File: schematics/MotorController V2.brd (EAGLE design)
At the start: 120.6 x 100 mm, 40 parts, among them IC1 7805, Q1 BC307

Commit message: AfterWeekend
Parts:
- removed HALL1, HALL2, HALL3: (no value), con-molex-micro-fit-3_0:43045-0612
- added D10, D11, D12, D13, D4, D5, D6, D7, D8, D9: 5.1V, diode:DO41Z10
- added D3: 1N5818-B, diode:DO41-7.6
- added R12, R13, R14: 1K, resistor:0204/7
- C1: value 2200uF -> 1000uF; device rcl:E7,5-16 -> rcl:E5-10,5
- C2: value 2200uF -> 100uF; device rcl:E7,5-16 -> rcl:E5-5
- CONTROL, S1, S2: value (none) -> (none)
- R1, R2, R3: value 330 -> 1K
- moved C3 79.2 mm to (0.00, 1.27), turned to 90 degrees
- moved R7 53.2 mm to (-34.9, 3.81), turned to 0 degrees
- moved R8 53.2 mm to (-34.9, 6.35), turned to 0 degrees
- moved R9 53.2 mm to (-34.9, 8.89), turned to 0 degrees
- moved R6 32.5 mm to (-35.6, 39.4), turned to 0 degrees
- moved R4 32.5 mm to (-35.6, 34.3), turned to 0 degrees
- moved R5 32.5 mm to (-35.6, 36.8), turned to 0 degrees
- moved IC1 22.2 mm to (8.89, 2.54), turned to 270 degrees
- moved R3 17.3 mm to (-35.6, 69.8), turned to 0 degrees
- moved R1 17.3 mm to (-35.6, 64.8), turned to 0 degrees
- moved R2 17.3 mm to (-35.6, 67.3), turned to 0 degrees
- moved C2 14.9 mm to (-2.54, -5.08), turned to 0 degrees
- moved POWER_IN 7.62 mm to (-16.5, -5.08)
- moved R11 6.35 mm to (-22.9, -5.08)
- moved U$2 5.39 mm to (11.4, 22.9), turned to 180 degrees
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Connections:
- net LCTRL-GND renamed CTRL-GND
- net N$48 renamed IMU-INT
- removed net LCTR-RX: CONTROL.6, U$2.HV4
- removed net LCTRL-SCL: CONTROL.4, U$2.HV2
- removed net LCTRL-SDA: CONTROL.3, U$2.HV1
- removed net LCTRL-TX: CONTROL.5, U$2.HV3
- removed net LCTRL-VDD: CONTROL.2, U$2.HV
- removed net LV: U$2.LV
- removed net N$49: HALL3.P$2, PRJ1.23/A9
- removed net N$50: HALL3.P$3, PRJ1.22/A8
- removed net N$51: HALL2.P$2, PRJ1.21/A7
- removed net N$54: HALL1.P$1, PRJ1.17/A3
- removed net N$55: HALL2.P$1, PRJ1.16/A2
- removed net N$56: HALL3.P$1, PRJ1.15/A1
- removed net N$57: HALL1.P$2, PRJ1.1/TX
- removed net N$58: HALL1.P$3, PRJ1.14/A0
- removed net N$59: HALL2.P$3, PRJ1.13/SCK
- new net CTR-SCL: CONTROL.4, U$2.LV1
- new net CTR-SDA: CONTROL.3, U$2.LV2
- new net CTRL-RX: CONTROL.6, U$2.LV4
- new net CTRL-TX: CONTROL.5, U$2.LV3
- new net CTRL-VDD: CONTROL.2, U$2.LV
- new net N$43: DRK1.EN, R12.2
- new net N$46: D4.C, PRJ1.24, R12.1, R13.1, R14.1
- new net N$48: DRK2.EN, R13.2
- net 3.3V: now also U$2.HV; no longer HALL1.P$5, HALL2.P$5, HALL3.P$5
- net GND: now also D10.A, D11.A, D12.A, D13.A, D4.A, D5.A, D6.A, D7.A, D8.A, D9.A; no longer HALL1.P$4, HALL2.P$4, HALL3.P$4
- net IMU-SCL: now also PRJ1.18/A4/SDA; no longer PRJ1.19/A5/SCL
- net IMU-SDA: now also PRJ1.19/A5/SCL; no longer PRJ1.18/A4/SDA
- net N$10: now also R14.2; no longer DRK1.EN, DRK2.EN, PRJ1.24
- net N$21: now also D8.C
- net N$22: now also D9.C
- net N$23: now also D10.C
- net N$27: now also D11.C
- net N$28: now also D12.C
- net N$29: now also D13.C
- net N$32: now also D3.C
- net N$34: now also ENCODER1.1; no longer ENCODER1.2
- net N$36: now also ENCODER2.1; no longer ENCODER2.2
- net N$38: now also ENCODER3.1; no longer ENCODER3.2
- net N$7: now also D7.C
- net N$8: now also D6.C
- net N$9: now also D5.C
- net RX5: now also U$2.HV4; no longer U$2.LV4
- net SCL1: now also U$2.HV1; no longer U$2.LV1
- net SDA1: now also U$2.HV2; no longer U$2.LV2
- net TX5: now also U$2.HV3; no longer U$2.LV3
- net VCC: now also D3.A, ENCODER1.2, ENCODER2.2, ENCODER3.2; no longer ENCODER1.1, ENCODER2.1, ENCODER3.1
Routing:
- net N$50: track 261.6 -> 0.00 mm, vias 3 -> 0
- net 3.3V: track 315.4 -> 105.4 mm, vias 3 -> 2
- net N$56: track 200.8 -> 0.00 mm, vias 3 -> 0
- net N$49: track 175.8 -> 0.00 mm, vias 3 -> 0
- net N$59: track 164.9 -> 0.00 mm, vias 3 -> 0
- net N$27: track 6.68 -> 164.7 mm
- net N$55: track 153.5 -> 0.00 mm, vias 1 -> 0
- net N$46: track 0.00 -> 139.6 mm, vias 0 -> 1
- net N$58: track 118.5 -> 0.00 mm, vias 3 -> 0
- net N$51: track 114.9 -> 0.00 mm, vias 3 -> 0
- net N$57: track 113.5 -> 0.00 mm, vias 2 -> 0
- net N$54: track 112.2 -> 0.00 mm, vias 2 -> 0
- net N$10: track 92.0 -> 2.08 mm, vias 2 -> 0
- net N$28: track 6.70 -> 78.9 mm, vias 0 -> 3
- net N$44: track 103.9 -> 175.1 mm, vias 2 -> 0
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
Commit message: no message
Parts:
- D10, D11, D12, D13, D4, D5, D6, D7, D8, D9: value 5.1V -> 5.6V
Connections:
- removed net N$41: PRJ1.32/A13, U$1.VDD
- net LIPO-GND: no longer U$1.D1
- net VCC: no longer U$1.!D2
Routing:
- net N$41: track 135.4 -> 0.00 mm, vias 3 -> 0
- net LIPO-GND: track 266.0 -> 263.1 mm
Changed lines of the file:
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@@
 <element name="D3" library="diode" library_urn="urn:adsk.eagle:library:210" package="DO41-7.6" package3d_urn="urn:adsk.eagle:package:43421/1" value="1N5818-B" x="-9.525" y="1.27"/>
 <element name="R12" library="resistor" library_urn="urn:adsk.eagle:library:348" package="0204/7" package3d_urn="urn:adsk.eagle:package:23498/1" value="1K" x="-35.56" y="72.39"/>
-<element name="D4" library="diode" library_urn="urn:adsk.eagle:library:210" package="DO41Z10" package3d_urn="urn:adsk.eagle:package:43341/1" value="5.1V" x="-46.355" y="72.39" rot="R180"/>
-<element name="D5" library="diode" library_urn="urn:adsk.eagle:library:210" package="DO41Z10" package3d_urn="urn:adsk.eagle:package:43341/1" value="5.1V" x="-46.355" y="69.85" rot="R180"/>
-<element name="D6" library="diode" library_urn="urn:adsk.eagle:library:210" package="DO41Z10" package3d_urn="urn:adsk.eagle:package:43341/1" value="5.1V" x="-46.355" y="67.31" rot="R180"/>
-<element name="D7" library="diode" library_urn="urn:adsk.eagle:library:210" package="DO41Z10" package3d_urn="urn:adsk.eagle:package:43341/1" value="5.1V" x="-46.355" y="64.77" rot="R180"/>
+<element name="D4" library="diode" library_urn="urn:adsk.eagle:library:210" package="DO41Z10" package3d_urn="urn:adsk.eagle:package:43341/1" value="5.6V" x="-46.355" y="72.39" rot="R180"/>
+<element name="D5" library="diode" library_urn="urn:adsk.eagle:library:210" package="DO41Z10" package3d_urn="urn:adsk.eagle:package:43341/1" value="5.6V" x="-46.355" y="69.85" rot="R180"/>
+<element name="D6" library="diode" library_urn="urn:adsk.eagle:library:210" package="DO41Z10" package3d_urn="urn:adsk.eagle:package:43341/1" value="5.6V" x="-46.355" y="67.31" rot="R180"/>
+<element name="D7" library="diode" library_urn="urn:adsk.eagle:library:210" package="DO41Z10" package3d_urn="urn:adsk.eagle:package:43341/1" value="5.6V" x="-46.355" y="64.77" rot="R180"/>
 <element name="R13" library="resistor" library_urn="urn:adsk.eagle:library:348" package="0204/7" package3d_urn="urn:adsk.eagle:package:23498/1" value="1K" x="-35.56" y="41.91"/>
 <element name="R14" library="resistor" library_urn="urn:adsk.eagle:library:348" package="0204/7" package3d_urn="urn:adsk.eagle:package:23498/1" value="1K" x="-34.925" y="11.43"/>
-<element name="D8" library="diode" library_urn="urn:adsk.eagle:library:210" package="DO41Z10" package3d_urn="urn:adsk.eagle:package:43341/1" value="5.1V" x="-46.355" y="39.37" rot="R180"/>
-<element name="D9" library="diode" library_urn="urn:adsk.eagle:library:210" package="DO41Z10" package3d_urn="urn:adsk.eagle:package:43341/1" value="5.1V" x="-46.355" y="36.83" rot="R180"/>
-<element name="D10" library="diode" library_urn="urn:adsk.eagle:library:210" package="DO41Z10" package3d_urn="urn:adsk.eagle:package:43341/1" value="5.1V" x="-46.355" y="34.29" rot="R180"/>
-<element name="D11" library="diode" library_urn="urn:adsk.eagle:library:210" package="DO41Z10" package3d_urn="urn:adsk.eagle:package:43341/1" value="5.1V" x="-46.355" y="8.89" rot="R180"/>
-<element name="D12" library="diode" library_urn="urn:adsk.eagle:library:210" package="DO41Z10" package3d_urn="urn:adsk.eagle:package:43341/1" value="5.1V" x="-46.355" y="6.35" rot="R180"/>
-<element name="D13" library="diode" library_urn="urn:adsk.eagle:library:210" package="DO41Z10" package3d_urn="urn:adsk.eagle:package:43341/1" value="5.1V" x="-46.355" y="3.81" rot="R180"/>
+<element name="D8" library="diode" library_urn="urn:adsk.eagle:library:210" package="DO41Z10" package3d_urn="urn:adsk.eagle:package:43341/1" value="5.6V" x="-46.355" y="39.37" rot="R180"/>
+<element name="D9" library="diode" library_urn="urn:adsk.eagle:library:210" package="DO41Z10" package3d_urn="urn:adsk.eagle:package:43341/1" value="5.6V" x="-46.355" y="36.83" rot="R180"/>
+<element name="D10" library="diode" library_urn="urn:adsk.eagle:library:210" package="DO41Z10" package3d_urn="urn:adsk.eagle:package:43341/1" value="5.6V" x="-46.355" y="34.29" rot="R180"/>
+<element name="D11" library="diode" library_urn="urn:adsk.eagle:library:210" package="DO41Z10" package3d_urn="urn:adsk.eagle:package:43341/1" value="5.6V" x="-46.355" y="8.89" rot="R180"/>
+<element name="D12" library="diode" library_urn="urn:adsk.eagle:library:210" package="DO41Z10" package3d_urn="urn:adsk.eagle:package:43341/1" value="5.6V" x="-46.355" y="6.35" rot="R180"/>
+<element name="D13" library="diode" library_urn="urn:adsk.eagle:library:210" package="DO41Z10" package3d_urn="urn:adsk.eagle:package:43341/1" value="5.6V" x="-46.355" y="3.81" rot="R180"/>
 </elements>
 <signals>
@@
 <contactref element="Q1" pad="1"/>
 <contactref element="U$1" pad="VIN"/>
-<contactref element="U$1" pad="!D2"/>
 <contactref element="ENCODER3" pad="2"/>
 <contactref element="ENCODER2" pad="2"/>
@@
 <wire x1="7.112" y1="66.675" x2="8.89" y2="64.897" width="0.254" layer="16"/>
 <wire x1="7.112" y1="77.56525" x2="7.112" y2="66.675" width="0.254" layer="16"/>
-<wire x1="8.89" y1="64.897" x2="8.89" y2="64.77" width="0.254" layer="16"/>
 <wire x1="25.3365" y1="50.673" x2="25.3365" y2="39.5605" width="0.254" layer="1"/>
 <wire x1="11.33475" y1="64.67475" x2="25.3365" y2="50.673" width="0.254" layer="1"/>
 <wire x1="8.89" y1="64.67475" x2="11.33475" y2="64.67475" width="0.254" layer="1"/>
 <wire x1="25.3365" y1="39.5605" x2="25.4" y2="39.37" width="0.254" layer="1"/>
-<wire x1="8.89" y1="64.67475" x2="8.89" y2="64.77" width="0.254" layer="1"/>
 <wire x1="24.66975" y1="0" x2="5.08" y2="0" width="0.254" layer="1"/>
 <wire x1="40.4495" y1="15.77975" x2="24.66975" y2="0" width="0.254" layer="1"/>
@@
 <via x="12.446" y="74.45375" extent="1-16" drill="0.635"/>
 <via x="-21.11375" y="-8.22325" extent="1-16" drill="0.635"/>
+<wire x1="8.89" y1="64.67475" x2="8.89" y2="64.897" width="0" layer="19" extent="1-16"/>
 </signal>
 <signal name="GND">
@@
 <wire x1="30.226" y1="58.45175" x2="30.099" y2="58.293" width="1" layer="1"/>
 </signal>
-<signal name="N$41">
-<contactref element="PRJ1" pad="32/A13"/>
-<contactref element="U$1" pad="VDD"/>
-<wire x1="-3.33375" y1="18.89125" x2="-15.113" y2="18.89125" width="0.254" layer="16"/>
-<wire x1="2.44475" y1="13.11275" x2="-3.33375" y2="18.89125" width="0.254" layer="16"/>
-<wire x1="39.116" y1="13.11275" x2="2.44475" y2="13.11275" width="0.254" layer="16"/>
-<wire x1="41.3385" y1="15.33525" x2="39.116" y2="13.11275" width="0.254" layer="16"/>
-<wire x1="41.3385" y1="28.8925" x2="41.3385" y2="15.33525" width="0.254" layer="16"/>
-<wire x1="39.33825" y1="30.89275" x2="41.3385" y2="28.8925" width="0.254" layer="16"/>
-<wire x1="34.671" y1="30.89275" x2="39.33825" y2="30.89275" width="0.254" layer="16"/>
-<wire x1="30.89275" y1="30.89275" x2="34.671" y2="30.89275" width="0.254" layer="1"/>
-<wire x1="23.114" y1="38.6715" x2="30.89275" y2="30.89275" width="0.254" layer="1"/>
-<wire x1="23.114" y1="50.89525" x2="23.114" y2="38.6715" width="0.254" layer="1"/>
-<wire x1="23.114" y1="58.00725" x2="23.114" y2="50.89525" width="0.254" layer="16"/>
-<wire x1="8.89" y1="72.23125" x2="23.114" y2="58.00725" width="0.254" layer="1"/>
-<wire x1="-15.113" y1="18.89125" x2="-15.24" y2="19.05" width="0.254" layer="16"/>
-<wire x1="8.89" y1="72.23125" x2="8.89" y2="72.39" width="0.254" layer="1"/>
-<via x="34.671" y="30.89275" extent="1-16" drill="0.635"/>
-<via x="23.114" y="50.89525" extent="1-16" drill="0.635"/>
-<via x="23.114" y="58.00725" extent="1-16" drill="0.635"/>
-</signal>
 <signal name="CTRL-RX">
 <contactref element="CONTROL" pad="6"/>
@@
 <contactref element="R11" pad="1"/>
 <contactref element="U$1" pad="GND"/>
-<contactref element="U$1" pad="D1"/>
 <wire x1="21.7805" y1="61.56325" x2="30.00375" y2="61.56325" width="1" layer="16"/>
 <wire x1="17.11325" y1="56.896" x2="21.7805" y2="61.56325" width="1" layer="16"/>
 <wire x1="11.77925" y1="62.23" x2="17.11325" y2="56.896" width="1" layer="1"/>
-<wire x1="8.89" y1="62.23" x2="11.77925" y2="62.23" width="1" layer="1"/>
 <wire x1="30.00375" y1="61.56325" x2="30.099" y2="61.722" width="1" layer="16"/>
 <wire x1="-38.6715" y1="-5.55625" x2="-38.6715" y2="-4.8895" width="1" layer="1"/>

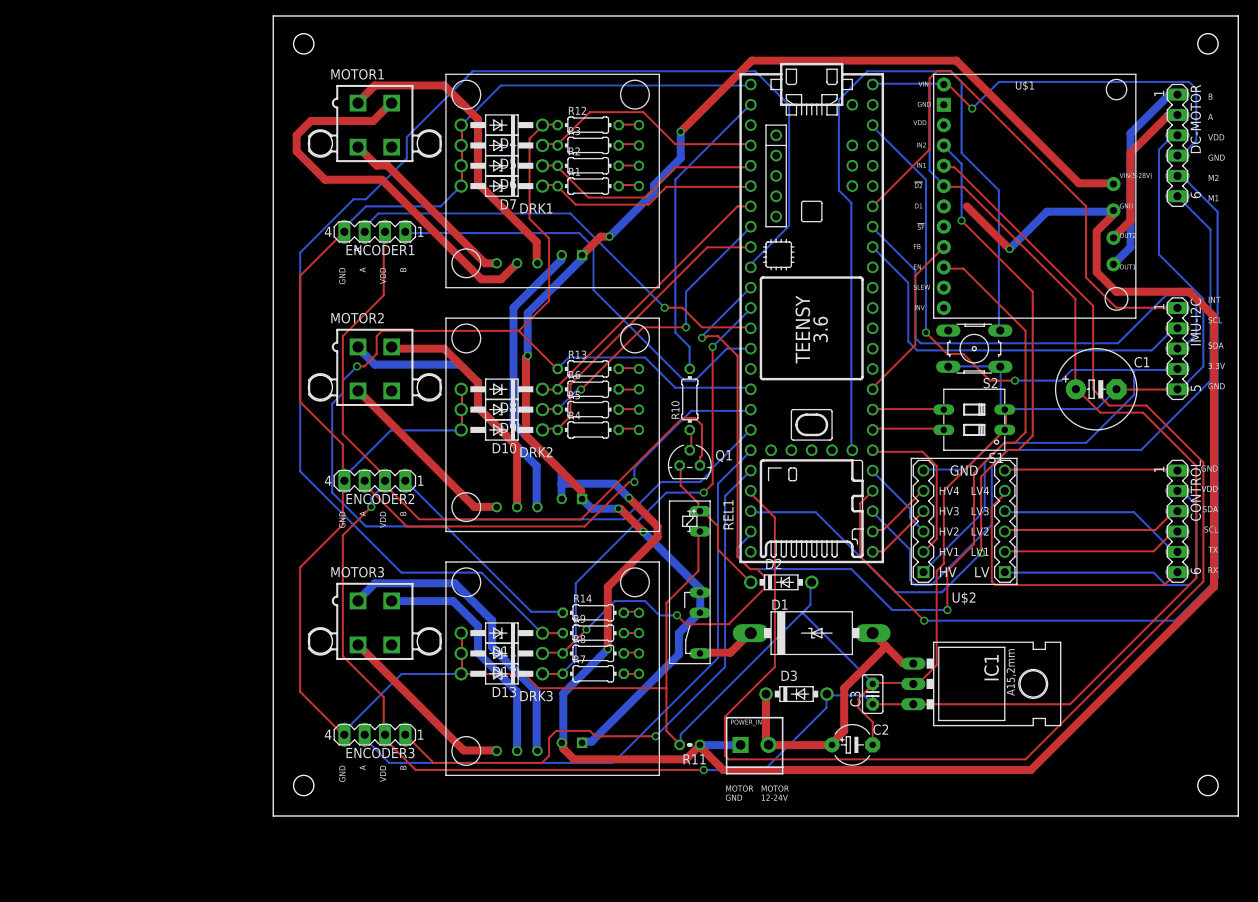
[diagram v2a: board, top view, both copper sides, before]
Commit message: accelerated bldc setup
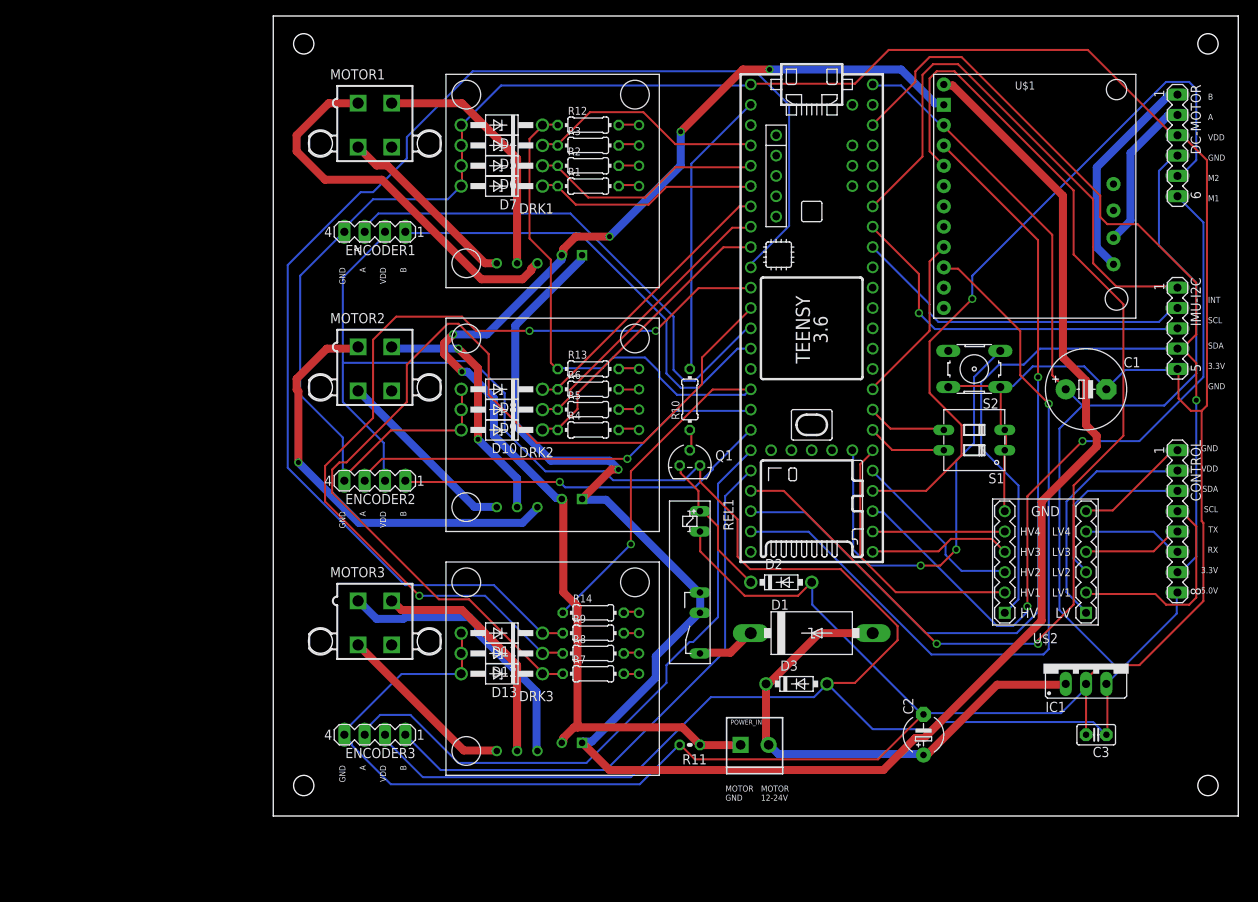
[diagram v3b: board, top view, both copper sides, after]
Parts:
- CONTROL: device con-lstb:MA06-1 -> con-lstb:MA08-1
- IC1: device v-reg:78XXL -> v-reg:78XXS
- moved C3 28.4 mm to (27.9, -3.81), turned to 180 degrees
- moved IC1 18.0 mm to (26.7, 5.08), turned to 0 degrees
- moved U$2 11.4 mm to (21.6, 17.8)
- moved C2 8.98 mm to (6.35, -3.81), turned to 90 degrees
- moved S2 2.54 mm to (12.7, 41.9)
- moved IMU-I2C 2.54 mm to (38.1, 47.0)
- moved S1 2.54 mm to (12.7, 33.0)
- moved D3 1.27 mm to (-9.53, 2.54)
- moved C1 1.27 mm to (26.7, 39.4)
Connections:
- removed net 3.3V: IMU-I2C.4, PRJ1.3V3_LO, U$2.HV
- removed net VCC: C1.+, C3.1, D3.A, DC-MOTOR.4, ENCODER1.2, ENCODER2.2, ENCODER3.2, IC1.OUT, PRJ1.VIN, Q1.1, U$1.VIN
- new net CTRL-3.3V: CONTROL.7, IMU-I2C.4, PRJ1.3V3_LO, U$2.HV
- new net CTRL-5.0V: C1.+, C3.1, CONTROL.8, D3.A, DC-MOTOR.4, ENCODER1.2, ENCODER2.2, ENCODER3.2, IC1.OUT, PRJ1.VIN, Q1.1, U$1.VDD(5V)
- net LIPO-GND: now also U$1.GND1; no longer U$1.GND
- net LIPO-VDD: now also U$1.VIN2(5-28V); no longer U$1.VIN(5-28V)
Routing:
- net CTRL-5.0V: track 0.00 -> 399.2 mm
- net VCC: track 373.1 -> 0.00 mm, vias 3 -> 0
- net CTRL-3.3V: track 0.00 -> 155.8 mm, vias 0 -> 1
- net 3.3V: track 105.4 -> 0.00 mm, vias 2 -> 0
- net LIPO-GND: track 263.1 -> 161.8 mm, vias 3 -> 5
- net GND: track 414.7 -> 490.6 mm
- net LIPO-VDD: track 167.1 -> 236.1 mm, vias 5 -> 1
- net N$29: track 60.5 -> 121.9 mm, vias 2 -> 0
- net N$52: track 95.0 -> 54.1 mm, vias 0 -> 2
- net N$46: track 139.6 -> 102.3 mm
- net N$28: track 78.9 -> 111.7 mm
- net N$44: track 175.1 -> 143.7 mm, vias 0 -> 2
- net N$32: track 36.1 -> 65.0 mm
- net CTRL-RX: track 36.1 -> 12.5 mm
- net Y_ENC_A: track 111.7 -> 89.8 mm
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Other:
- board text added: "5.0V"

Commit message: no message
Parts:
- added U$3: NODEMCU, nodemcu:NODEMCU
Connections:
- new net 3V: U$3.11, U$3.16, U$3.25
- net GND: now also U$3.10, U$3.14, U$3.17, U$3.2, U$3.24
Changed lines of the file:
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@@
 <element name="D12" library="diode" library_urn="urn:adsk.eagle:library:210" package="DO41Z10" package3d_urn="urn:adsk.eagle:package:43341/1" value="5.6V" x="-46.355" y="6.35" rot="R180"/>
 <element name="D13" library="diode" library_urn="urn:adsk.eagle:library:210" package="DO41Z10" package3d_urn="urn:adsk.eagle:package:43341/1" value="5.6V" x="-46.355" y="3.81" rot="R180"/>
+<element name="U$3" library="nodemcu" package="NODEMCU" value="NODEMCU" x="-91.44" y="17.78"/>
 </elements>
 <signals>
@@
 <wire x1="-15.113" y1="77.56525" x2="-15.24" y2="77.47" width="0.254" layer="1"/>
 <wire x1="38.00475" y1="71.12" x2="38.1" y2="71.12" width="0.254" layer="1"/>
+<contactref element="U$3" pad="2"/>
+<contactref element="U$3" pad="10"/>
+<contactref element="U$3" pad="14"/>
+<contactref element="U$3" pad="17"/>
+<contactref element="U$3" pad="24"/>
+<wire x1="-105.41" y1="12.7" x2="-105.41" y2="2.54" width="0" layer="19" extent="1-1"/>
+<wire x1="-105.41" y1="33.02" x2="-105.41" y2="12.7" width="0" layer="19" extent="1-1"/>
+<wire x1="-77.47" y1="2.54" x2="-105.41" y2="2.54" width="0" layer="19" extent="1-1"/>
+<wire x1="-66.00825" y1="-3.33375" x2="-77.47" y2="2.54" width="0" layer="19" extent="16-16"/>
+<wire x1="-77.47" y1="20.32" x2="-66.2305" y2="28.0035" width="0" layer="19" extent="16-16"/>
 </signal>
 <signal name="N$4">
@@
 <wire x1="-29.337" y1="42.00525" x2="-29.21" y2="41.91" width="0.254" layer="1"/>
 </signal>
+<signal name="3V">
+<contactref element="U$3" pad="11"/>
+<contactref element="U$3" pad="16"/>
+<contactref element="U$3" pad="25"/>
+<wire x1="-77.47" y1="0" x2="-105.41" y2="10.16" width="0" layer="19" extent="1-1"/>
+<wire x1="-77.47" y1="22.86" x2="-77.47" y2="0" width="0" layer="19" extent="1-1"/>
+</signal>
 </signals>
